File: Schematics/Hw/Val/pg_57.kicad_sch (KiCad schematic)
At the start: 23 parts, among them U5901 F74, U5902 F74, U5903 F74, U5904 F74, U5905 F74, U5906 F74, U5907 F74, U5908 F74, U5909 F74, U5910 F74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

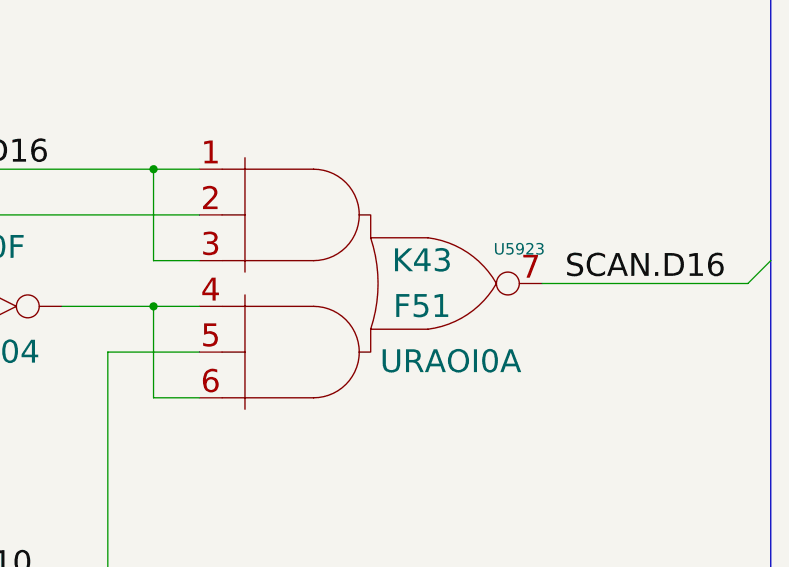
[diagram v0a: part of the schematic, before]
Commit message: Upgrade to KiCad9
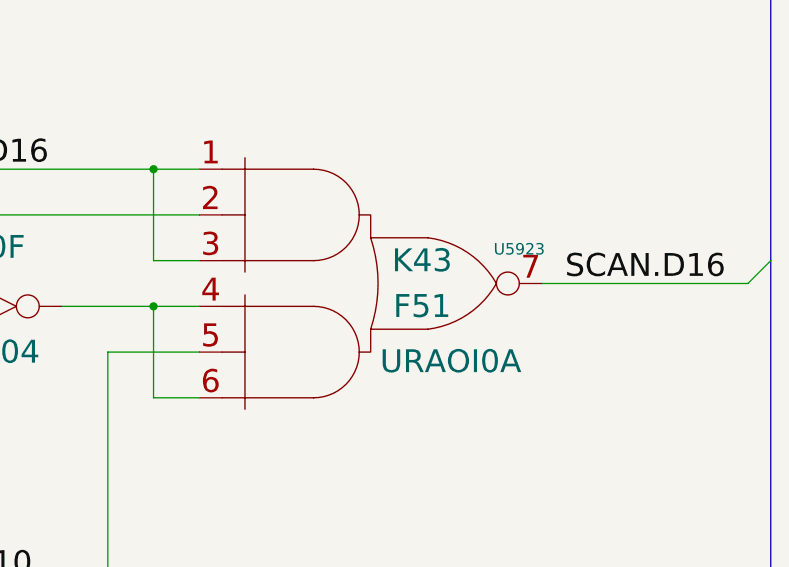
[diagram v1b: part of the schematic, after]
